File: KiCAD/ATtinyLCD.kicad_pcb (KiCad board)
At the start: 2 copper layers, 59.4 x 30 mm, 9 parts, among them IC1 74164, IC2 ATtiny13-20PU, IC3 DHT22, J1 Screw_Terminal_01x02, U1 NHD-0420H1Z

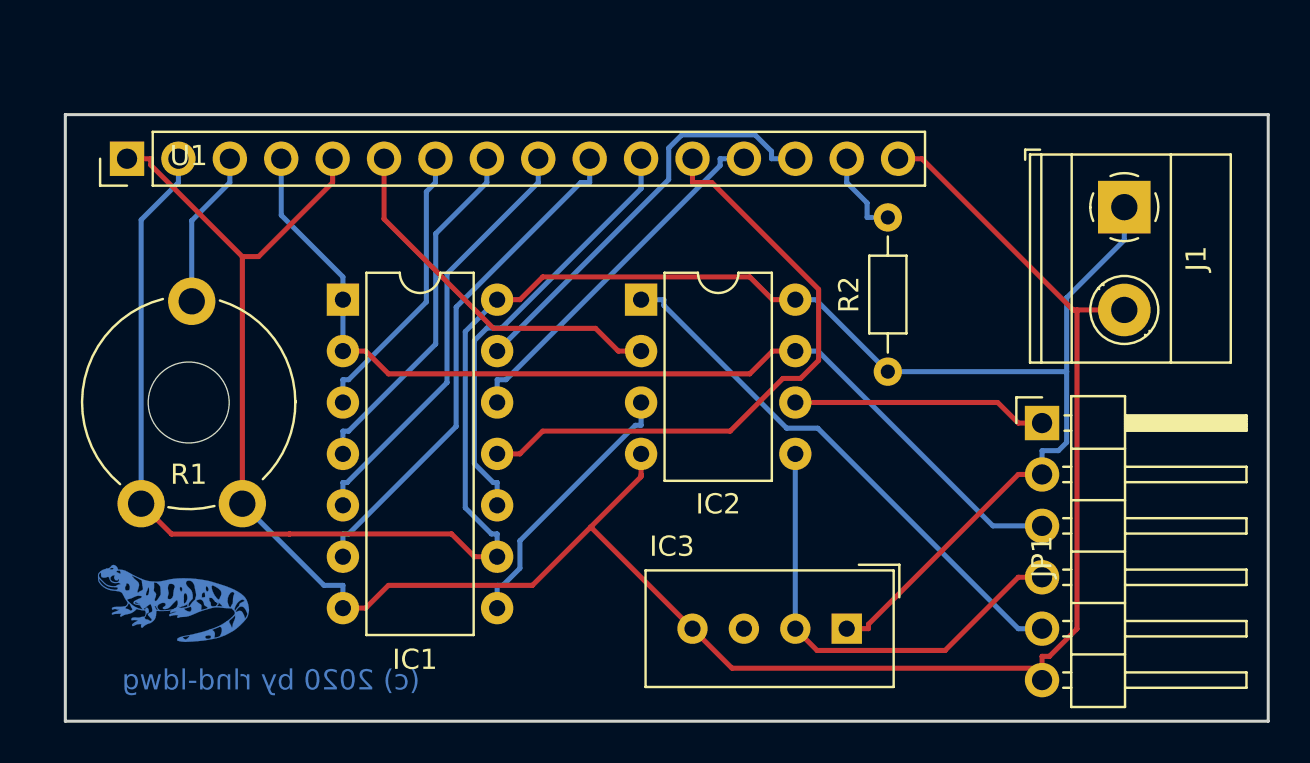
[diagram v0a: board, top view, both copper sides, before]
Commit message: v1.0.5 corrected error in pcb
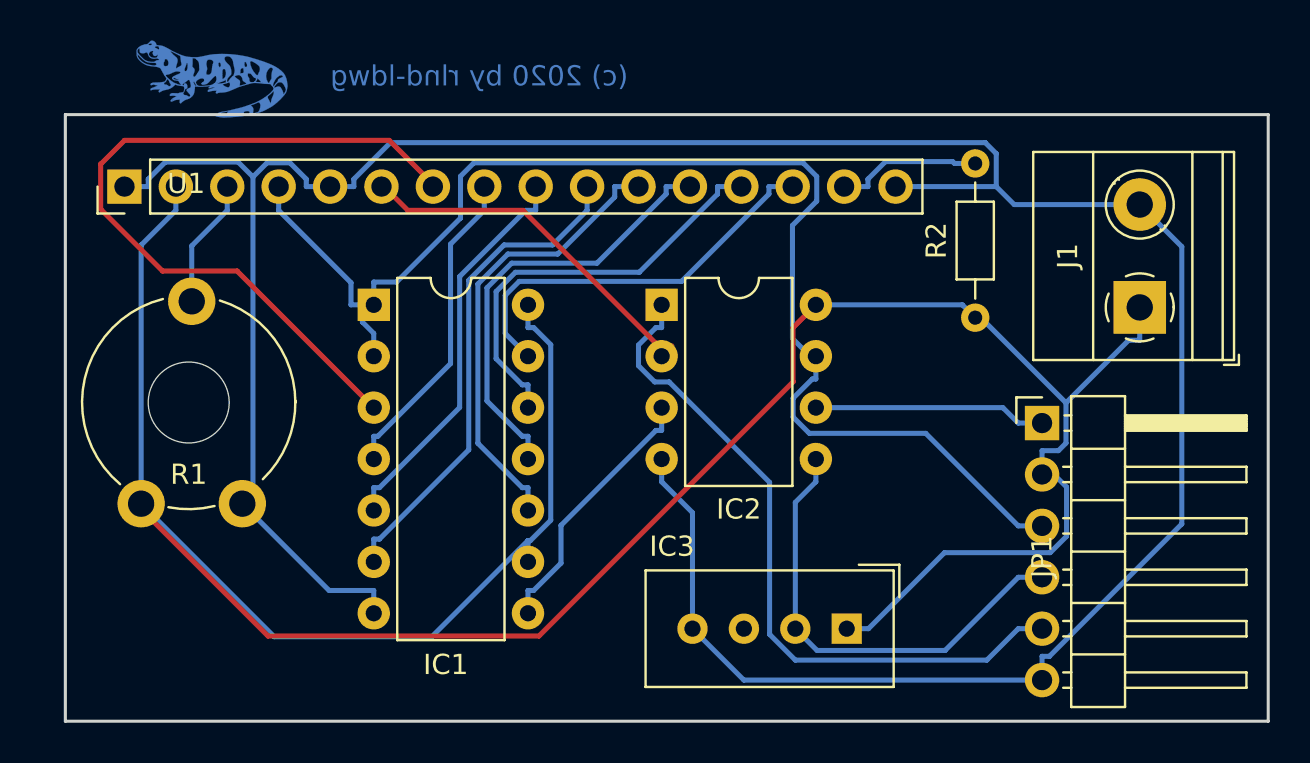
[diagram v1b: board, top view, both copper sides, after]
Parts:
- moved G*** 26.0 mm to (28.1, 18.5)
- moved R2 5.08 mm to (65.8, 30.4)
- moved J1 5.01 mm to (73.9, 29.8), turned to 90 degrees
- moved IC1 1.55 mm to (36.1, 29.7)
- moved U1 1.38 mm to (23.7, 23.9)
- moved IC2 1.05 mm to (50.3, 29.7)
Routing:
- net +5V: track 109.6 -> 142.0 mm
- net GND: track 112.2 -> 141.0 mm
- net Net-(IC1-Pad3): track 14.1 -> 37.4 mm
- net Net-(IC1-Pad1): track 49.8 -> 66.4 mm
- net Net-(IC1-Pad11): track 30.9 -> 21.8 mm
- net Net-(IC2-Pad1): track 26.7 -> 34.7 mm
- net Net-(IC1-Pad12): track 18.0 -> 21.0 mm
- net Net-(R2-Pad2): track 4.34 -> 7.24 mm
- net Net-(IC1-Pad4): track 17.7 -> 15.8 mm
- net Net-(IC1-Pad5): track 21.2 -> 19.8 mm
- net Net-(R1-Pad2): track 7.82 -> 6.39 mm
- net Net-(IC2-Pad2): track 18.4 -> 17.1 mm
- net Net-(IC2-Pad6): track 12.6 -> 11.5 mm
- net Net-(IC1-Pad10): track 21.5 -> 22.6 mm
- net Net-(IC1-Pad6): track 25.1 -> 24.5 mm
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
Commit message: v1.0.6 correction of display errors of single-digit values, minor modifications on schematic and pcb
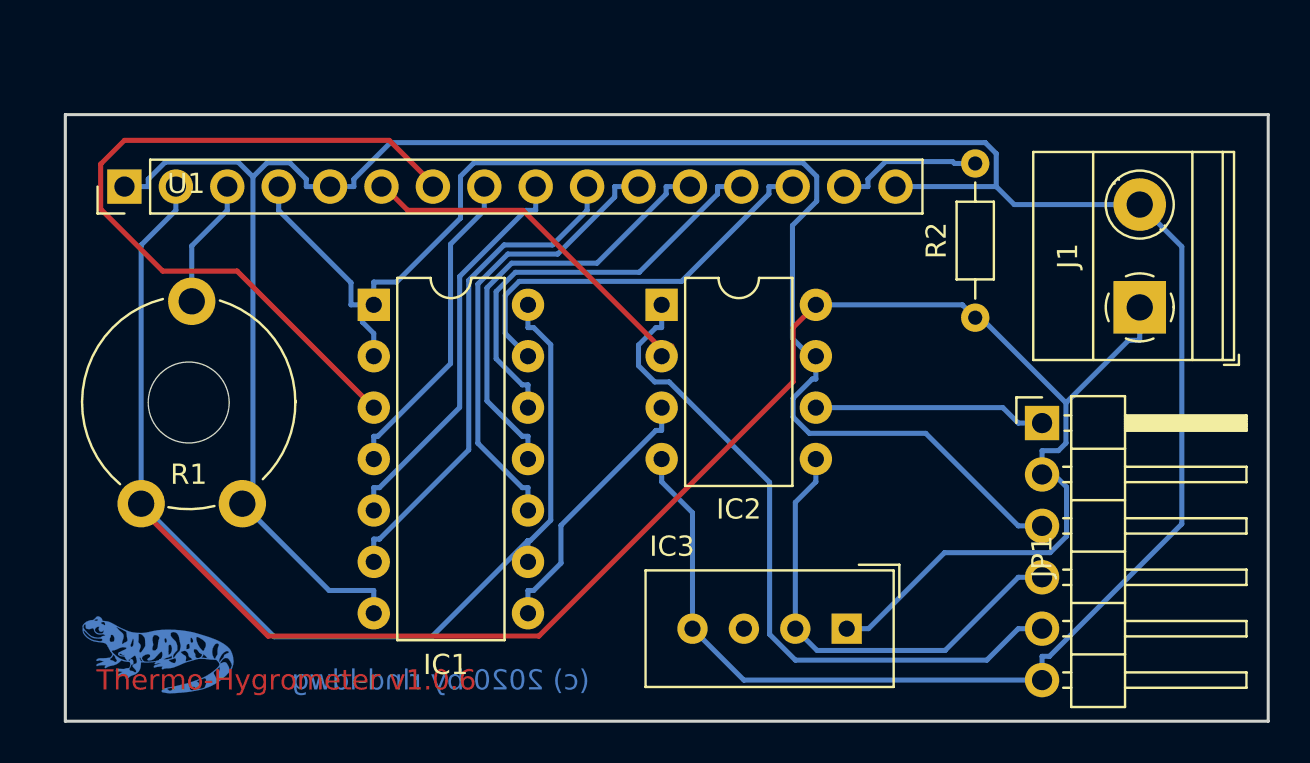
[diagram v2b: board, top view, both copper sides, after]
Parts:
- moved G*** 28.6 mm to (25.4, 47.0)
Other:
- board text added: "Thermo-Hygrometer v1.0.6"
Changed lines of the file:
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@@
-(kicad_pcb (version 20171130) (host pcbnew 5.1.8+dfsg1-1~bpo10+1)
+(kicad_pcb (version 20171130) (host pcbnew 5.1.7)
   (general
     (thickness 1.6)
-    (drawings 5)
+    (drawings 6)
     (tracks 206)
     (zones 0)
@@
   )
   (module my:Logomini (layer F.Cu)
-    (at 28.067 18.542)
+    (at 25.4 46.99)
     (fp_text reference G*** (at 0 0) (layer F.SilkS) hide
       (effects (font (size 1.524 1.524) (thickness 0.3)))
@@
     )
   )
-  (gr_text "(c) 2020 by rlnd-ldwg" (at 41.275 18.415) (layer B.Cu)
+  (gr_text "Thermo-Hygrometer v1.0.6" (at 31.75 48.26) (layer F.Cu)
+    (effects (font (size 1 1) (thickness 0.15)))
+  )
+  (gr_text "(c) 2020 by rlnd-ldwg" (at 39.37 48.26) (layer B.Cu)
     (effects (font (size 1 1) (thickness 0.15)) (justify mirror))
   )
